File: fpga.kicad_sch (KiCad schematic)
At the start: 10 parts, among them U10 P0082_BOTTOMMOUNT, Y1 XLL735080.000000I

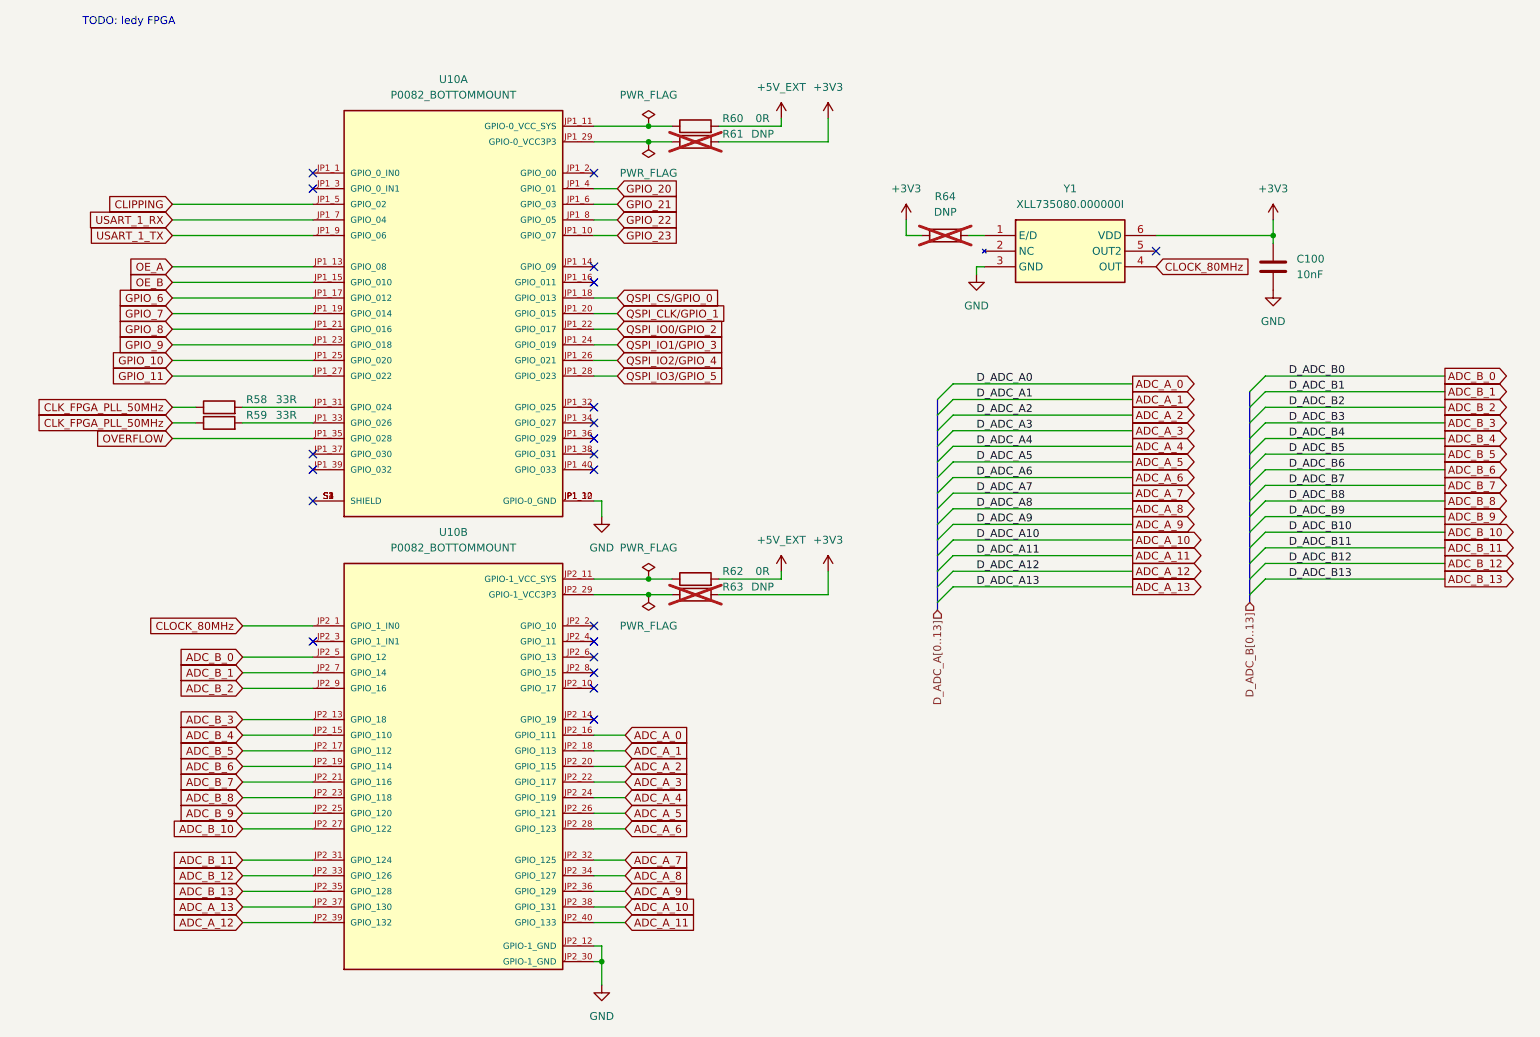
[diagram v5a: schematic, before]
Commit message: Fix fpga ADC pin assignment
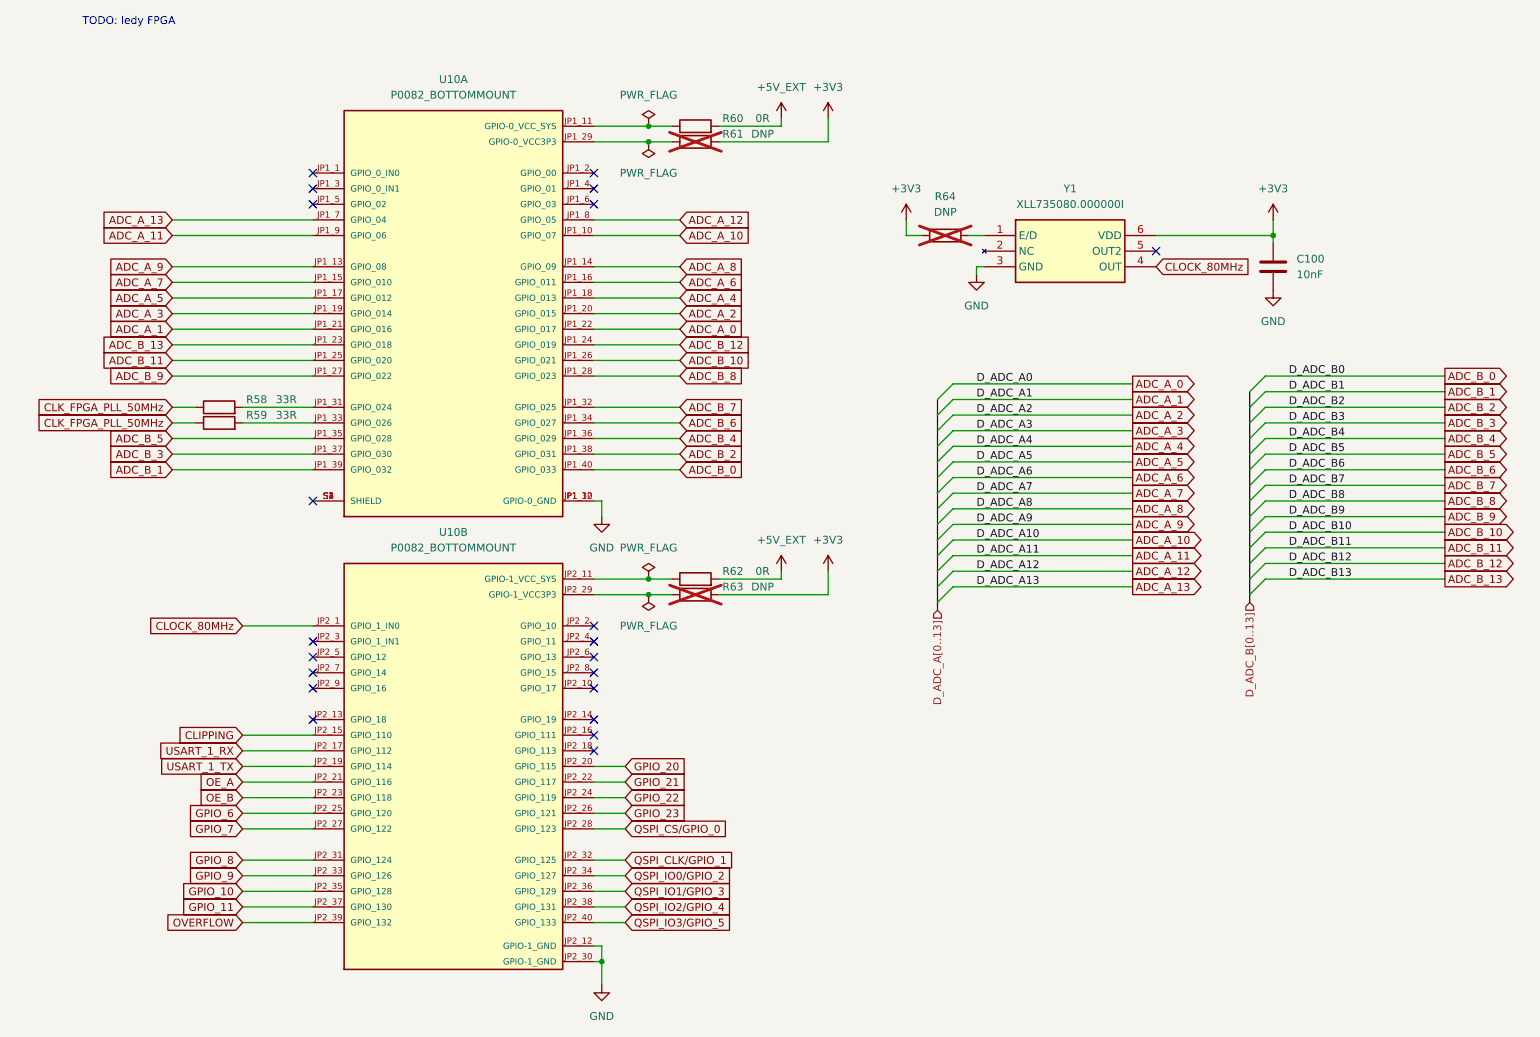
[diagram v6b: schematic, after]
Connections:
- net ADC_A_0: now also U10.JP1_22 (GPIO_017); no longer U10.JP2_16 (GPIO_111)
- net ADC_A_1: now also U10.JP1_21 (GPIO_016); no longer U10.JP2_18 (GPIO_113)
- net ADC_A_10: now also U10.JP1_10 (GPIO_07); no longer U10.JP2_38 (GPIO_131)
- net ADC_A_11: now also U10.JP1_9 (GPIO_06); no longer U10.JP2_40 (GPIO_133)
- net ADC_A_12: now also U10.JP1_8 (GPIO_05); no longer U10.JP2_39 (GPIO_132)
- net ADC_A_13: now also U10.JP1_7 (GPIO_04); no longer U10.JP2_37 (GPIO_130)
- net ADC_A_2: now also U10.JP1_20 (GPIO_015); no longer U10.JP2_20 (GPIO_115)
- net ADC_A_3: now also U10.JP1_19 (GPIO_014); no longer U10.JP2_22 (GPIO_117)
- net ADC_A_4: now also U10.JP1_18 (GPIO_013); no longer U10.JP2_24 (GPIO_119)
- net ADC_A_5: now also U10.JP1_17 (GPIO_012); no longer U10.JP2_26 (GPIO_121)
- net ADC_A_6: now also U10.JP1_16 (GPIO_011); no longer U10.JP2_28 (GPIO_123)
- net ADC_A_7: now also U10.JP1_15 (GPIO_010); no longer U10.JP2_32 (GPIO_125)
- net ADC_A_8: now also U10.JP1_14 (GPIO_09); no longer U10.JP2_34 (GPIO_127)
- net ADC_A_9: now also U10.JP1_13 (GPIO_08); no longer U10.JP2_36 (GPIO_129)
- net ADC_B_0: now also U10.JP1_40 (GPIO_033); no longer U10.JP2_5 (GPIO_12)
- net ADC_B_1: now also U10.JP1_39 (GPIO_032); no longer U10.JP2_7 (GPIO_14)
- net ADC_B_10: now also U10.JP1_26 (GPIO_021); no longer U10.JP2_27 (GPIO_122)
- net ADC_B_11: now also U10.JP1_25 (GPIO_020); no longer U10.JP2_31 (GPIO_124)
- net ADC_B_12: now also U10.JP1_24 (GPIO_019); no longer U10.JP2_33 (GPIO_126)
- net ADC_B_13: now also U10.JP1_23 (GPIO_018); no longer U10.JP2_35 (GPIO_128)
- net ADC_B_2: now also U10.JP1_38 (GPIO_031); no longer U10.JP2_9 (GPIO_16)
- net ADC_B_3: now also U10.JP1_37 (GPIO_030); no longer U10.JP2_13 (GPIO_18)
- net ADC_B_4: now also U10.JP1_36 (GPIO_029); no longer U10.JP2_15 (GPIO_110)
- net ADC_B_5: now also U10.JP1_35 (GPIO_028); no longer U10.JP2_17 (GPIO_112)
- net ADC_B_6: now also U10.JP1_34 (GPIO_027); no longer U10.JP2_19 (GPIO_114)
- net ADC_B_7: now also U10.JP1_32 (GPIO_025); no longer U10.JP2_21 (GPIO_116)
- net ADC_B_8: now also U10.JP1_28 (GPIO_023); no longer U10.JP2_23 (GPIO_118)
- net ADC_B_9: now also U10.JP1_27 (GPIO_022); no longer U10.JP2_25 (GPIO_120)
- net CLIPPING: now also U10.JP2_15 (GPIO_110); no longer U10.JP1_5 (GPIO_02)
- net GPIO_10: now also U10.JP2_35 (GPIO_128); no longer U10.JP1_25 (GPIO_020)
- net GPIO_11: now also U10.JP2_37 (GPIO_130); no longer U10.JP1_27 (GPIO_022)
- net GPIO_20: now also U10.JP2_20 (GPIO_115); no longer U10.JP1_4 (GPIO_01)
- net GPIO_21: now also U10.JP2_22 (GPIO_117); no longer U10.JP1_6 (GPIO_03)
- net GPIO_22: now also U10.JP2_24 (GPIO_119); no longer U10.JP1_8 (GPIO_05)
- net GPIO_23: now also U10.JP2_26 (GPIO_121); no longer U10.JP1_10 (GPIO_07)
- net GPIO_6: now also U10.JP2_25 (GPIO_120); no longer U10.JP1_17 (GPIO_012)
- net GPIO_7: now also U10.JP2_27 (GPIO_122); no longer U10.JP1_19 (GPIO_014)
- net GPIO_8: now also U10.JP2_31 (GPIO_124); no longer U10.JP1_21 (GPIO_016)
- net GPIO_9: now also U10.JP2_33 (GPIO_126); no longer U10.JP1_23 (GPIO_018)
- net OE_A: now also U10.JP2_21 (GPIO_116); no longer U10.JP1_13 (GPIO_08)
- net OE_B: now also U10.JP2_23 (GPIO_118); no longer U10.JP1_15 (GPIO_010)
- net OVERFLOW: now also U10.JP2_39 (GPIO_132); no longer U10.JP1_35 (GPIO_028)
- net QSPI_CLK/GPIO_1: now also U10.JP2_32 (GPIO_125); no longer U10.JP1_20 (GPIO_015)
- net QSPI_CS/GPIO_0: now also U10.JP2_28 (GPIO_123); no longer U10.JP1_18 (GPIO_013)
- net QSPI_IO0/GPIO_2: now also U10.JP2_34 (GPIO_127); no longer U10.JP1_22 (GPIO_017)
- net QSPI_IO1/GPIO_3: now also U10.JP2_36 (GPIO_129); no longer U10.JP1_24 (GPIO_019)
- net QSPI_IO2/GPIO_4: now also U10.JP2_38 (GPIO_131); no longer U10.JP1_26 (GPIO_021)
- net QSPI_IO3/GPIO_5: now also U10.JP2_40 (GPIO_133); no longer U10.JP1_28 (GPIO_023)
- net USART_1_RX: now also U10.JP2_17 (GPIO_112); no longer U10.JP1_7 (GPIO_04)
- net USART_1_TX: now also U10.JP2_19 (GPIO_114); no longer U10.JP1_9 (GPIO_06)

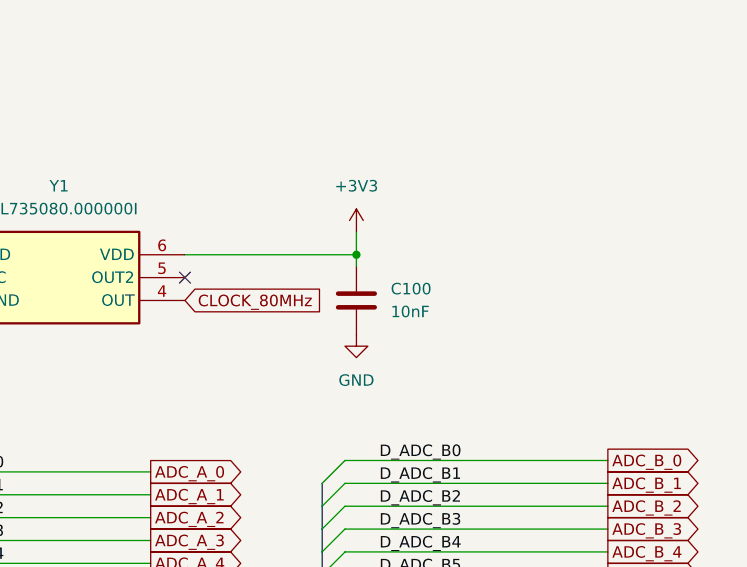
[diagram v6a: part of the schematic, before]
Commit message: Add LDO's
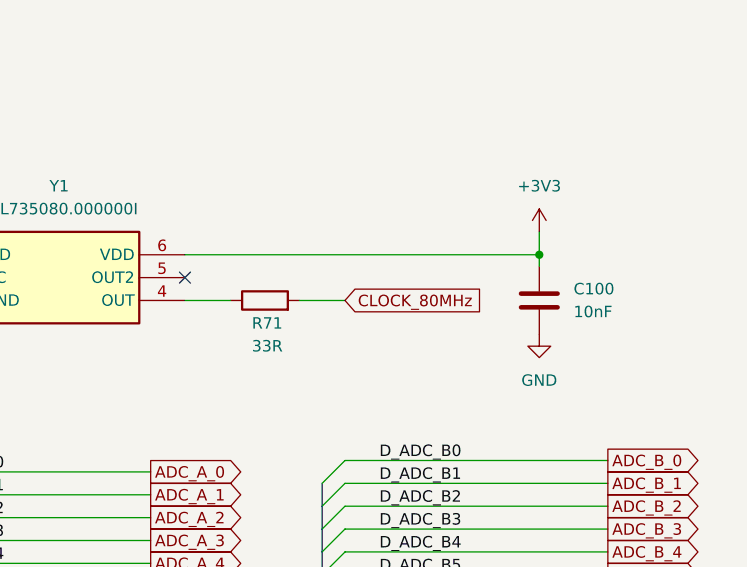
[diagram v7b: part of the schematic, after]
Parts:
- added R71: 33R, Resistor_SMD:R_0805_2012Metric, symbol Device:R
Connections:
- net CLOCK_80MHz: now also R71.2; no longer Y1.4 (OUT)
- new net: R71.1, Y1.4 (OUT)
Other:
- moved on the sheet: C100
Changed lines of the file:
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@@
 	)
 	(junction
-		(at 236.22 57.15)
+		(at 256.54 57.15)
 		(diameter 0)
 		(color 0 0 0 0)
@@
 	(wire
 		(pts
-			(xy 236.22 57.15) (xy 236.22 58.42)
+			(xy 256.54 57.15) (xy 256.54 58.42)
 		)
 		(stroke
@@
 	(wire
 		(pts
+			(xy 217.17 62.23) (xy 222.25 62.23)
+		)
+		(stroke
+			(width 0)
+			(type default)
+		)
+	)
+	(wire
+		(pts
 			(xy 57.15 72.39) (xy 80.01 72.39)
 		)
@@
 	(wire
 		(pts
-			(xy 236.22 54.61) (xy 236.22 57.15)
+			(xy 256.54 54.61) (xy 256.54 57.15)
 		)
 		(stroke
@@
 	(wire
 		(pts
-			(xy 217.17 57.15) (xy 236.22 57.15)
+			(xy 68.58 166.37) (xy 80.01 166.37)
 		)
 		(stroke
@@
 	(wire
 		(pts
-			(xy 68.58 166.37) (xy 80.01 166.37)
+			(xy 234.95 82.55) (xy 264.16 82.55)
 		)
 		(stroke
@@
 	(wire
 		(pts
-			(xy 234.95 82.55) (xy 264.16 82.55)
+			(xy 130.81 166.37) (xy 125.73 166.37)
 		)
 		(stroke
@@
 	(wire
 		(pts
-			(xy 130.81 166.37) (xy 125.73 166.37)
+			(xy 184.15 114.3) (xy 213.36 114.3)
 		)
 		(stroke
@@
 	(wire
 		(pts
-			(xy 184.15 114.3) (xy 213.36 114.3)
+			(xy 57.15 95.25) (xy 80.01 95.25)
 		)
 		(stroke
@@
 	(wire
 		(pts
-			(xy 57.15 95.25) (xy 80.01 95.25)
+			(xy 229.87 62.23) (xy 234.95 62.23)
 		)
 		(stroke
@@
 	(wire
 		(pts
+			(xy 217.17 57.15) (xy 256.54 57.15)
+		)
+		(stroke
+			(width 0)
+			(type default)
+		)
+	)
+	(wire
+		(pts
 			(xy 139.7 77.47) (xy 125.73 77.47)
 		)
@@
 	(global_label "CLOCK_80MHz"
 		(shape input)
-		(at 217.17 62.23 0)
+		(at 234.95 62.23 0)
 		(fields_autoplaced yes)
 		(effects
@@
 		)
 		(property "Intersheetrefs" "${INTERSHEET_REFS}"
-			(at 233.5204 62.23 0)
+			(at 251.3004 62.23 0)
 			(effects
 				(font
@@
 	(symbol
 		(lib_id "power:GND")
-		(at 236.22 66.04 0)
+		(at 256.54 66.04 0)
 		(unit 1)
 		(exclude_from_sim no)
@@
 		(fields_autoplaced yes)
 		(property "Reference" "#PWR0148"
-			(at 236.22 72.39 0)
+			(at 256.54 72.39 0)
 			(effects
 				(font
@@
 		)
 		(property "Value" "GND"
-			(at 236.22 71.12 0)
+			(at 256.54 71.12 0)
 			(effects
 				(font
@@
 		)
 		(property "Footprint" ""
-			(at 236.22 66.04 0)
+			(at 256.54 66.04 0)
 			(effects
 				(font
@@
 		)
 		(property "Datasheet" ""
-			(at 236.22 66.04 0)
+			(at 256.54 66.04 0)
 			(effects
 				(font
@@
 		)
 		(property "Description" "Power symbol creates a global label with name \"GND\" , ground"
-			(at 236.22 66.04 0)
+			(at 256.54 66.04 0)
 			(effects
 				(font
@@
 	)
 	(symbol
+		(lib_id "Device:R")
+		(at 226.06 62.23 90)
+		(unit 1)
+		(exclude_from_sim no)
+		(in_bom yes)
+		(on_board yes)
+		(dnp no)
+		(property "Reference" "R71"
+			(at 226.314 64.77 90)
+			(effects
+				(font
+					(size 1.27 1.27)
+				)
+			)
+		)
+		(property "Value" "33R"
+			(at 226.314 67.31 90)
+			(effects
+				(font
+					(size 1.27 1.27)
+				)
+			)
+		)
+		(property "Footprint" "Resistor_SMD:R_0805_2012Metric"
+			(at 226.06 64.008 90)
+			(effects
+				(font
+					(size 1.27 1.27)
+				)
+				(hide yes)
+			)
+		)
+		(property "Datasheet" "~"
+			(at 226.06 62.23 0)
+			(effects
+				(font
+					(size 1.27 1.27)
+				)
+				(hide yes)
+			)
+		)
+		(property "Description" "Resistor"
+			(at 226.06 62.23 0)
+			(effects
+				(font
+					(size 1.27 1.27)
+				)
+				(hide yes)
+			)
+		)
+		(pin "2"
+		)
+		(pin "1"
+		)
+		(instances
+			(project ""
+				(path "/553deb7b-4100-40fe-99d2-0c7b4b56aad2/3a7288c4-cf21-495b-9b8e-7b87b52ff1d8"
+					(reference "R71")
+					(unit 1)
+				)
+			)
+		)
+	)
+	(symbol
 		(lib_id "power:GND")
 		(at 127 179.07 0)
@@
 	(symbol
 		(lib_id "power:+3V3")
-		(at 236.22 54.61 0)
+		(at 256.54 54.61 0)
 		(unit 1)
 		(exclude_from_sim no)
@@
 		(fields_autoplaced yes)
 		(property "Reference" "#PWR0147"
-			(at 236.22 58.42 0)
+			(at 256.54 58.42 0)
 			(effects
 				(font
@@
 		)
 		(property "Value" "+3V3"
-			(at 236.22 49.53 0)
+			(at 256.54 49.53 0)
 			(effects
 				(font
@@
 		)
 		(property "Footprint" ""
-			(at 236.22 54.61 0)
+			(at 256.54 54.61 0)
 			(effects
 				(font
@@
 		)
 		(property "Datasheet" ""
-			(at 236.22 54.61 0)
+			(at 256.54 54.61 0)
 			(effects
 				(font
@@
 		)
 		(property "Description" "Power symbol creates a global label with name \"+3V3\""
-			(at 236.22 54.61 0)
+			(at 256.54 54.61 0)
 			(effects
 				(font
@@
 	(symbol
 		(lib_id "Device:C")
-		(at 236.22 62.23 0)
+		(at 256.54 62.23 0)
 		(unit 1)
 		(exclude_from_sim no)
@@
 		(fields_autoplaced yes)
 		(property "Reference" "C100"
-			(at 240.03 60.9599 0)
+			(at 260.35 60.9599 0)
 			(effects
 				(font
@@
 		)
 		(property "Value" "10nF"
-			(at 240.03 63.4999 0)
+			(at 260.35 63.4999 0)
 			(effects
 				(font
@@
 		)
 		(property "Footprint" "Capacitor_SMD:C_0805_2012Metric"
-			(at 237.1852 66.04 0)
+			(at 257.5052 66.04 0)
 			(effects
 				(font
@@
 		)
 		(property "Datasheet" "~"
-			(at 236.22 62.23 0)
+			(at 256.54 62.23 0)
 			(effects
 				(font
@@
 		)
 		(property "Description" "Unpolarized capacitor"
-			(at 236.22 62.23 0)
+			(at 256.54 62.23 0)
 			(effects
 				(font

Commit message: Do most of the PCB
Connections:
- net AN_TRIGGER_P: now reaches U10.JP2_3 (GPIO_1_IN1)
- net AN_TRIGGER_N: now reaches U10.JP2_5 (GPIO_12)
- no-connect marks 21 -> 19
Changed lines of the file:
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@@
-	)
-	(no_connect
-		(at 80.01 125.73)
 	)
 	(no_connect
@@
 	)
 	(no_connect
-		(at 80.01 123.19)
-	)
-	(no_connect
 		(at 125.73 138.43)
 	)
@@
 	(wire
 		(pts
+			(xy 68.58 125.73) (xy 80.01 125.73)
+		)
+		(stroke
+			(width 0)
+			(type default)
+		)
+	)
+	(wire
+		(pts
 			(xy 127 175.26) (xy 127 179.07)
 		)
@@
 		(pts
 			(xy 232.41 85.09) (xy 232.41 87.63)
+		)
+		(stroke
+			(width 0)
+			(type default)
+		)
+	)
+	(wire
+		(pts
+			(xy 68.58 123.19) (xy 80.01 123.19)
 		)
 		(stroke
@@
 		)
 	)
+	(global_label "AN_TRIGGER_N"
+		(shape input)
+		(at 68.58 125.73 180)
+		(fields_autoplaced yes)
+		(effects
+			(font
+				(size 1.27 1.27)
+			)
+			(justify right)
+		)
+		(property "Intersheetrefs" "${INTERSHEET_REFS}"
+			(at 52.1086 125.73 0)
+			(effects
+				(font
+					(size 1.27 1.27)
+				)
+				(justify right)
+				(hide yes)
+			)
+		)
+	)
 	(global_label "ADC_B_2"
 		(shape input)
@@
 				(hide yes)
 			)
+		)
+	)
+	(global_label "AN_TRIGGER_P"
+		(shape input)
+		(at 68.58 123.19 180)
+		(fields_autoplaced yes)
+		(effects
+			(font
+				(size 1.27 1.27)
+			)
+			(justify right)
+		)
+		(property "Intersheetrefs" "${INTERSHEET_REFS}"
+			(at 52.1691 123.19 0)
+			(effects
+				(font
+					(size 1.27 1.27)
+				)
+				(justify right)
+				(hide yes)
+			)
